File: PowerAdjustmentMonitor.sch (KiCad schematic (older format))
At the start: 0 parts

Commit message: try out power control
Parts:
- added C? (x2): C, ~, symbol C
- added R?: R, ~, symbol R
- added RV?: POT, ~, symbol POT
- added U?: LM317, ~, symbol LM317
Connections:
- new net: R?.2, RV?.2, U?.2 (ADJ)
- new net +12V: C?.1, U?.1 (IN)
- new net GND: C?.2, C?.2, RV?.1
- new net VAA: C?.1, R?.1, U?.3 (OUT)
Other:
- note added: "need some way to change this pot value with arduino..."
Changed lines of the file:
@@
 $Descr A4 11693 8268
 encoding utf-8
-Sheet 1 9
+Sheet 9 9
 Title ""
-Date "6 feb 2014"
+Date "7 feb 2014"
 Rev ""
 Comp ""
@@
 Comment4 ""
 $EndDescr
+$Comp
+L LM317 U?
+U 1 1 52F4C8CD
+P 5100 3450
+F 0 "U?" H 5100 3750 60  0000 C CNN
+F 1 "LM317" H 5150 3200 60  0000 L CNN
+F 2 "~" H 5100 3450 60  0000 C CNN
+F 3 "~" H 5100 3450 60  0000 C CNN
+	1    5100 3450
+	1    0    0    -1
+$EndComp
+$Comp
+L +12V #PWR?
+U 1 1 52F4C9AE
+P 4350 3000
+F 0 "#PWR?" H 4350 2950 20  0001 C CNN
+F 1 "+12V" H 4350 3100 30  0000 C CNN
+F 2 "" H 4350 3000 60  0000 C CNN
+F 3 "" H 4350 3000 60  0000 C CNN
+	1    4350 3000
+	1    0    0    -1
+$EndComp
+$Comp
+L GND #PWR?
+U 1 1 52F4C9BD
+P 6350 4550
+F 0 "#PWR?" H 6350 4550 30  0001 C CNN
+F 1 "GND" H 6350 4480 30  0001 C CNN
+F 2 "" H 6350 4550 60  0000 C CNN
+F 3 "" H 6350 4550 60  0000 C CNN
+	1    6350 4550
+	1    0    0    -1
+$EndComp
+$Comp
+L R R?
+U 1 1 52F4C9CC
+P 5900 3600
+F 0 "R?" V 5980 3600 40  0000 C CNN
+F 1 "R" V 5907 3601 40  0000 C CNN
+F 2 "~" V 5830 3600 30  0000 C CNN
+F 3 "~" H 5900 3600 30  0000 C CNN
+	1    5900 3600
+	1    0    0    -1
+$EndComp
+$Comp
+L C C?
+U 1 1 52F4C9E1
+P 6350 3550
+F 0 "C?" H 6350 3650 40  0000 L CNN
+F 1 "C" H 6356 3465 40  0000 L CNN
+F 2 "~" H 6388 3400 30  0000 C CNN
+F 3 "~" H 6350 3550 60  0000 C CNN
+	1    6350 3550
+	1    0    0    -1
+$EndComp
+Wire Wire Line
+	4350 3000 4350 3300
+Wire Wire Line
+	4350 3300 4700 3300
+Wire Wire Line
+	5500 3300 6700 3300
+Wire Wire Line
+	5900 3300 5900 3350
+Wire Wire Line
+	6350 3300 6350 3350
+Connection ~ 5900 3300
+Wire Wire Line
+	6350 3750 6350 4550
+Wire Wire Line
+	5900 3850 5900 4050
+Wire Wire Line
+	5900 3900 5100 3900
+Wire Wire Line
+	5100 3900 5100 3800
+Connection ~ 5900 3900
+$Comp
+L GND #PWR?
+U 1 1 52F4CA1B
+P 5600 4550
+F 0 "#PWR?" H 5600 4550 30  0001 C CNN
+F 1 "GND" H 5600 4480 30  0001 C CNN
+F 2 "" H 5600 4550 60  0000 C CNN
+F 3 "" H 5600 4550 60  0000 C CNN
+	1    5600 4550
+	1    0    0    -1
+$EndComp
+Wire Wire Line
+	5600 4200 5600 4550
+$Comp
+L C C?
+U 1 1 52F4CA2F
+P 4500 3550
+F 0 "C?" H 4500 3650 40  0000 L CNN
+F 1 "C" H 4506 3465 40  0000 L CNN
+F 2 "~" H 4538 3400 30  0000 C CNN
+F 3 "~" H 4500 3550 60  0000 C CNN
+	1    4500 3550
+	1    0    0    -1
+$EndComp
+$Comp
+L GND #PWR?
+U 1 1 52F4CA35
+P 4500 4500
+F 0 "#PWR?" H 4500 4500 30  0001 C CNN
+F 1 "GND" H 4500 4430 30  0001 C CNN
+F 2 "" H 4500 4500 60  0000 C CNN
+F 3 "" H 4500 4500 60  0000 C CNN
+	1    4500 4500
+	1    0    0    -1
+$EndComp
+Wire Wire Line
+	4500 4500 4500 3750
+Wire Wire Line
+	4500 3350 4500 3300
+Connection ~ 4500 3300
+$Comp
+L VAA #PWR?
+U 1 1 52F4CA58
+P 6700 3000
+F 0 "#PWR?" H 6700 3060 30  0001 C CNN
+F 1 "VAA" H 6700 3110 30  0000 C CNN
+F 2 "" H 6700 3000 60  0000 C CNN
+F 3 "" H 6700 3000 60  0000 C CNN
+	1    6700 3000
+	1    0    0    -1
+$EndComp
+Wire Wire Line
+	6700 3300 6700 3000
+Connection ~ 6350 3300
+$Comp
+L POT RV?
+U 1 1 52F4CA77
+P 5900 4200
+F 0 "RV?" H 5900 4100 50  0000 C CNN
+F 1 "POT" H 5900 4200 50  0000 C CNN
+F 2 "~" H 5900 4200 60  0000 C CNN
+F 3 "~" H 5900 4200 60  0000 C CNN
+	1    5900 4200
+	1    0    0    -1
+$EndComp
+Wire Wire Line
+	5600 4200 5650 4200
+Text Notes 4900 4900 0    60   ~ 0
+need some way to change this pot value with arduino...
 $EndSCHEMATC

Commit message: after power adjustment video
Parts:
- removed RV?: POT, ~, symbol POT
- added R? (x4): R, ~, symbol R
- added U?: LM324, symbol LM324
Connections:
- net labels added: +3,3V, +5V, -12V, 3V3_MON, 5V_MON, FE_V+, FE_V-, V+_ADJ, V+_ADJ_MON, V+_CURR_MON, V+_MON, V-_ADJ, V-_ADJ_MON, V-_CURR_MON
- wire segments 14 -> 39
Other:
- note added: "And the same for the negative rail"
- note removed: "need some way to change this pot value with arduino..."
- moved on the sheet: C?, R?, U?

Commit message: arduino module / hooking things up
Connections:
- net labels added: +3.3V
- net labels removed: +3,3V
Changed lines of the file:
@@
 Connection ~ 4950 1400
-$Comp
-L +3,3V #PWR?
-U 1 1 52F4D462
-P 6650 3450
-F 0 "#PWR?" H 6650 3410 30  0001 C CNN
-F 1 "+3,3V" H 6650 3560 30  0000 C CNN
-F 2 "" H 6650 3450 60  0000 C CNN
-F 3 "" H 6650 3450 60  0000 C CNN
-	1    6650 3450
-	1    0    0    -1
-$EndComp
 $Comp
 L +5V #PWR?
@@
 Text Notes 3000 6500 0    60   ~ 0
 And the same for the negative rail
+$Comp
+L +3.3V #PWR?
+U 1 1 52F5DC5C
+P 6650 3450
+F 0 "#PWR?" H 6650 3410 30  0001 C CNN
+F 1 "+3.3V" H 6650 3560 30  0000 C CNN
+F 2 "" H 6650 3450 60  0000 C CNN
+F 3 "" H 6650 3450 60  0000 C CNN
+	1    6650 3450
+	1    0    0    -1
+$EndComp
 $EndSCHEMATC

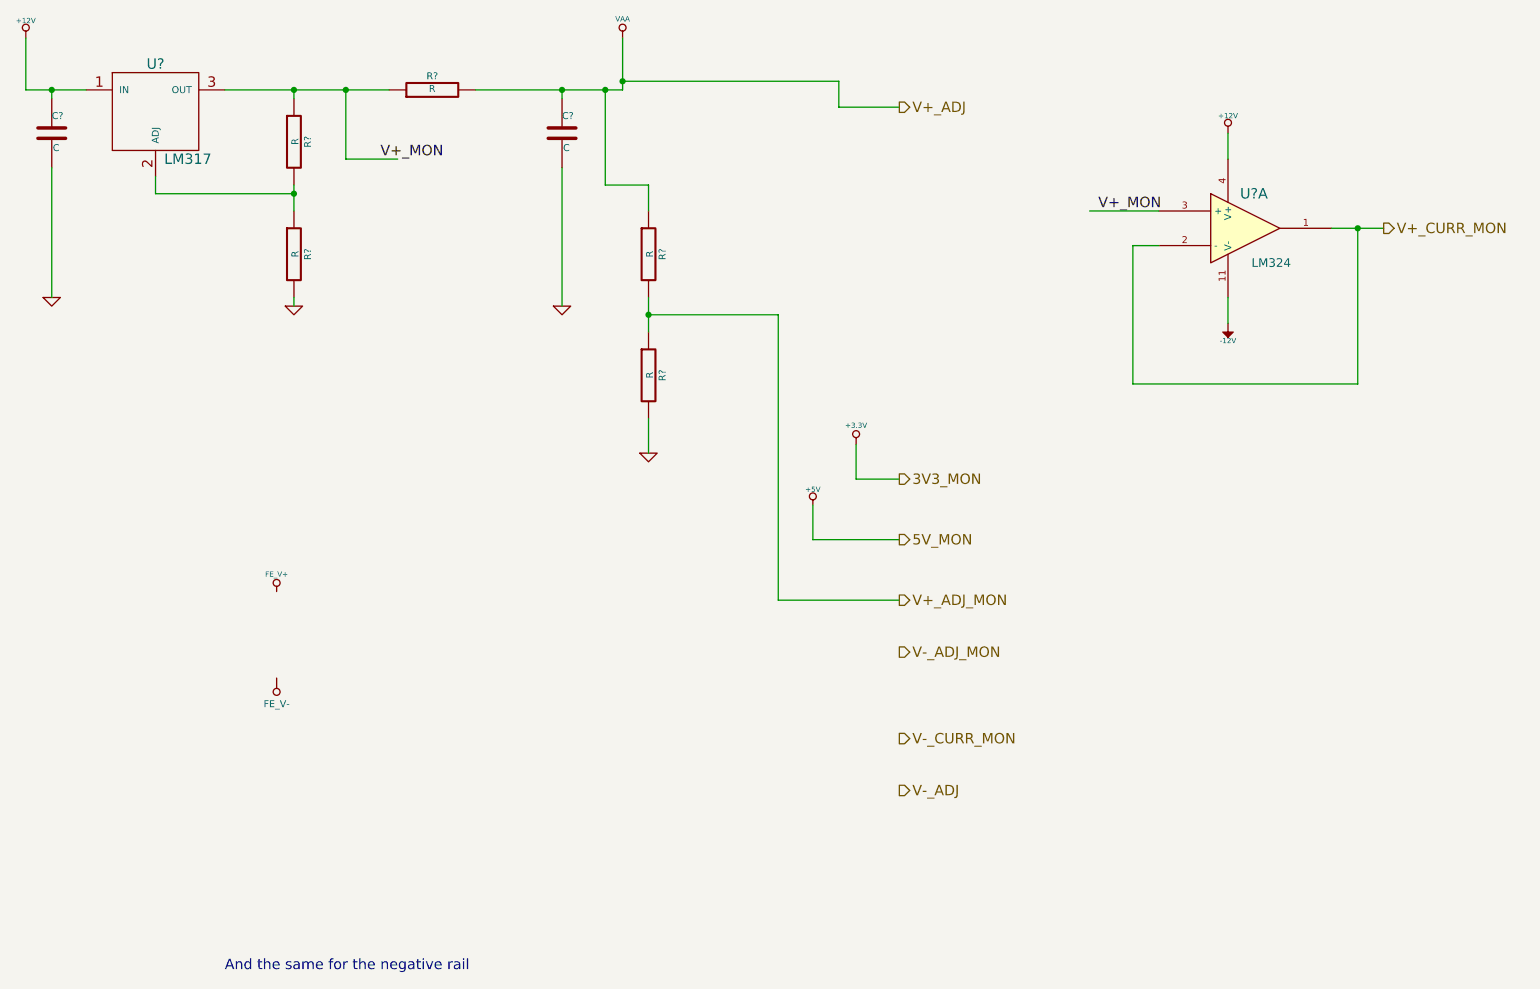
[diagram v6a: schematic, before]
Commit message: associating and placing relay module
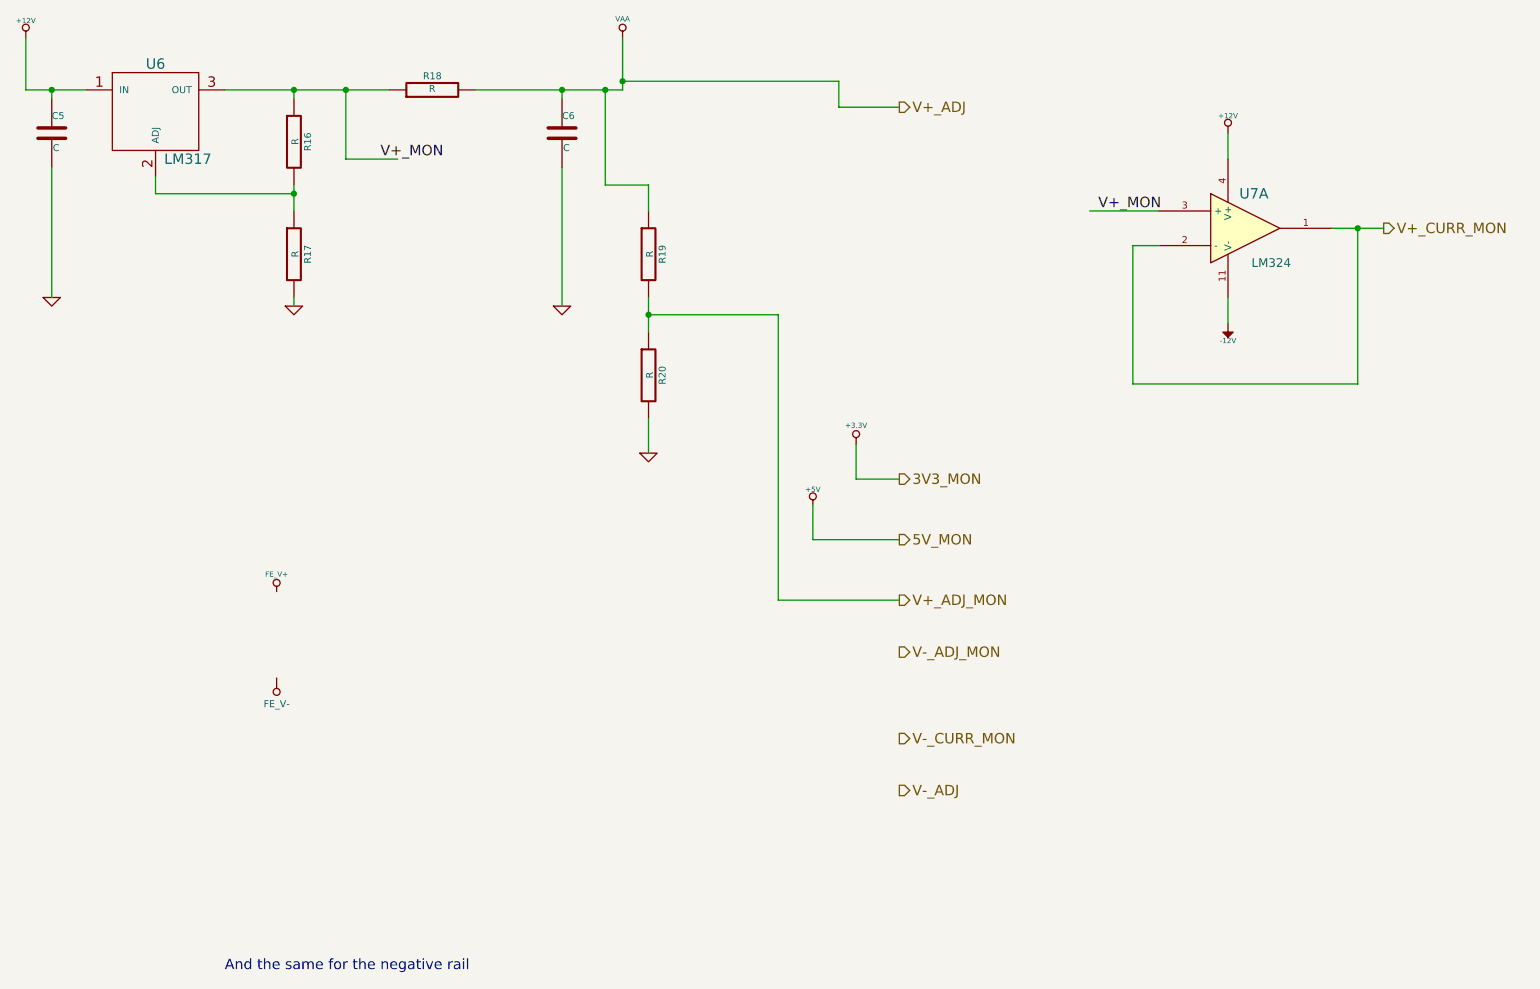
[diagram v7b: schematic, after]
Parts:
- gave numbers to parts that had none: 9
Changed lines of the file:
@@
 Sheet 7 9
 Title ""
-Date "10 feb 2014"
+Date "22 feb 2014"
 Rev ""
 Comp ""
@@
 $EndDescr
 $Comp
-L LM317 U?
+L LM317 U6
 U 1 1 52F4C8CD
 P 2600 1550
-F 0 "U?" H 2600 1850 60  0000 C CNN
+F 0 "U6" H 2600 1850 60  0000 C CNN
 F 1 "LM317" H 2650 1300 60  0000 L CNN
 F 2 "~" H 2600 1550 60  0000 C CNN
@@
 $EndComp
 $Comp
-L +12V #PWR?
+L +12V #PWR033
 U 1 1 52F4C9AE
 P 1850 1100
-F 0 "#PWR?" H 1850 1050 20  0001 C CNN
+F 0 "#PWR033" H 1850 1050 20  0001 C CNN
 F 1 "+12V" H 1850 1200 30  0000 C CNN
 F 2 "" H 1850 1100 60  0000 C CNN
@@
 $EndComp
 $Comp
-L GND #PWR?
+L GND #PWR034
 U 1 1 52F4C9BD
 P 4950 2650
-F 0 "#PWR?" H 4950 2650 30  0001 C CNN
+F 0 "#PWR034" H 4950 2650 30  0001 C CNN
 F 1 "GND" H 4950 2580 30  0001 C CNN
 F 2 "" H 4950 2650 60  0000 C CNN
@@
 $EndComp
 $Comp
-L R R?
+L R R16
 U 1 1 52F4C9CC
 P 3400 1700
-F 0 "R?" V 3480 1700 40  0000 C CNN
+F 0 "R16" V 3480 1700 40  0000 C CNN
 F 1 "R" V 3407 1701 40  0000 C CNN
 F 2 "~" V 3330 1700 30  0000 C CNN
@@
 $EndComp
 $Comp
-L C C?
+L C C6
 U 1 1 52F4C9E1
 P 4950 1650
-F 0 "C?" H 4950 1750 40  0000 L CNN
+F 0 "C6" H 4950 1750 40  0000 L CNN
 F 1 "C" H 4956 1565 40  0000 L CNN
 F 2 "~" H 4988 1500 30  0000 C CNN
@@
 Connection ~ 3400 2000
 $Comp
-L GND #PWR?
+L GND #PWR035
 U 1 1 52F4CA1B
 P 3400 2650
-F 0 "#PWR?" H 3400 2650 30  0001 C CNN
+F 0 "#PWR035" H 3400 2650 30  0001 C CNN
 F 1 "GND" H 3400 2580 30  0001 C CNN
 F 2 "" H 3400 2650 60  0000 C CNN
@@
 $EndComp
 $Comp
-L C C?
+L C C5
 U 1 1 52F4CA2F
 P 2000 1650
-F 0 "C?" H 2000 1750 40  0000 L CNN
+F 0 "C5" H 2000 1750 40  0000 L CNN
 F 1 "C" H 2006 1565 40  0000 L CNN
 F 2 "~" H 2038 1500 30  0000 C CNN
@@
 $EndComp
 $Comp
-L GND #PWR?
+L GND #PWR036
 U 1 1 52F4CA35
 P 2000 2600
-F 0 "#PWR?" H 2000 2600 30  0001 C CNN
+F 0 "#PWR036" H 2000 2600 30  0001 C CNN
 F 1 "GND" H 2000 2530 30  0001 C CNN
 F 2 "" H 2000 2600 60  0000 C CNN
@@
 Connection ~ 2000 1400
 $Comp
-L VAA #PWR?
+L VAA #PWR037
 U 1 1 52F4CA58
 P 5300 1100
-F 0 "#PWR?" H 5300 1160 30  0001 C CNN
+F 0 "#PWR037" H 5300 1160 30  0001 C CNN
 F 1 "VAA" H 5300 1210 30  0000 C CNN
 F 2 "" H 5300 1100 60  0000 C CNN
@@
 Connection ~ 4950 1400
 $Comp
-L +5V #PWR?
+L +5V #PWR038
 U 1 1 52F4D468
 P 6400 3800
-F 0 "#PWR?" H 6400 3890 20  0001 C CNN
+F 0 "#PWR038" H 6400 3890 20  0001 C CNN
 F 1 "+5V" H 6400 3890 30  0000 C CNN
 F 2 "" H 6400 3800 60  0000 C CNN
@@
 $EndComp
 $Comp
-L +12V #PWR?
+L +12V #PWR039
 U 1 1 52F4D504
 P 8800 1650
-F 0 "#PWR?" H 8800 1600 20  0001 C CNN
+F 0 "#PWR039" H 8800 1600 20  0001 C CNN
 F 1 "+12V" H 8800 1750 30  0000 C CNN
 F 2 "" H 8800 1650 60  0000 C CNN
@@
 $EndComp
 $Comp
-L -12V #PWR?
+L -12V #PWR040
 U 1 1 52F4D4FE
 P 8800 2750
-F 0 "#PWR?" H 8800 2880 20  0001 C CNN
+F 0 "#PWR040" H 8800 2880 20  0001 C CNN
 F 1 "-12V" H 8800 2850 30  0000 C CNN
 F 2 "" H 8800 2750 60  0000 C CNN
@@
 $EndComp
 $Comp
-L FE_V+ #PWR?
+L FE_V+ #PWR041
 U 1 1 52F4D55E
 P 3300 4300
-F 0 "#PWR?" H 3300 4400 30  0001 C CNN
+F 0 "#PWR041" H 3300 4400 30  0001 C CNN
 F 1 "FE_V+" H 3300 4400 30  0000 C CNN
 F 2 "" H 3300 4300 60  0000 C CNN
@@
 $EndComp
 $Comp
-L FE_V- #PWR?
+L FE_V- #PWR36
 U 1 1 52F4D56D
 P 3300 4800
-F 0 "#PWR?" H 3300 5000 40  0001 C CNN
+F 0 "#PWR36" H 3300 5000 40  0001 C CNN
 F 1 "FE_V-" H 3300 4950 40  0000 C CNN
 F 2 "" H 3300 4800 60  0000 C CNN
@@
 V-_CURR_MON
 $Comp
-L R R?
+L R R17
 U 1 1 52F4D69E
 P 3400 2350
-F 0 "R?" V 3480 2350 40  0000 C CNN
+F 0 "R17" V 3480 2350 40  0000 C CNN
 F 1 "R" V 3407 2351 40  0000 C CNN
 F 2 "~" V 3330 2350 30  0000 C CNN
@@
 	3400 2600 3400 2650
 $Comp
-L R R?
+L R R19
 U 1 1 52F4D6CF
 P 5450 2350
-F 0 "R?" V 5530 2350 40  0000 C CNN
+F 0 "R19" V 5530 2350 40  0000 C CNN
 F 1 "R" V 5457 2351 40  0000 C CNN
 F 2 "~" V 5380 2350 30  0000 C CNN
@@
 $EndComp
 $Comp
-L R R?
+L R R20
 U 1 1 52F4D6D5
 P 5450 3050
-F 0 "R?" V 5530 3050 40  0000 C CNN
+F 0 "R20" V 5530 3050 40  0000 C CNN
 F 1 "R" V 5457 3051 40  0000 C CNN
 F 2 "~" V 5380 3050 30  0000 C CNN
@@
 $EndComp
 $Comp
-L GND #PWR?
+L GND #PWR042
 U 1 1 52F4D6DB
 P 5450 3500
-F 0 "#PWR?" H 5450 3500 30  0001 C CNN
+F 0 "#PWR042" H 5450 3500 30  0001 C CNN
 F 1 "GND" H 5450 3430 30  0001 C CNN
 F 2 "" H 5450 3500 60  0000 C CNN
@@
 	6400 4000 6900 4000
 $Comp
-L R R?
+L R R18
 U 1 1 52F4D7CB
 P 4200 1400
-F 0 "R?" V 4280 1400 40  0000 C CNN
+F 0 "R18" V 4280 1400 40  0000 C CNN
 F 1 "R" V 4207 1401 40  0000 C CNN
 F 2 "~" V 4130 1400 30  0000 C CNN
@@
 V+_MON
 $Comp
-L LM324 U?
+L LM324 U7
 U 1 1 52F4D895
 P 8900 2200
-F 0 "U?" H 8950 2400 60  0000 C CNN
+F 0 "U7" H 8950 2400 60  0000 C CNN
 F 1 "LM324" H 9050 2000 50  0000 C CNN
 F 2 "" H 8900 2200 60  0000 C CNN
@@
 And the same for the negative rail
 $Comp
-L +3.3V #PWR?
+L +3.3V #PWR043
 U 1 1 52F5DC5C
 P 6650 3450
-F 0 "#PWR?" H 6650 3410 30  0001 C CNN
+F 0 "#PWR043" H 6650 3410 30  0001 C CNN
 F 1 "+3.3V" H 6650 3560 30  0000 C CNN
 F 2 "" H 6650 3450 60  0000 C CNN
